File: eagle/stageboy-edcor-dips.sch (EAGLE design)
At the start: 38 parts, among them IC1 MEGA8-P, IC2 7805TV, J2 DCJ0202, Q1 16MHz, X1 MIDI IN, X2 MIDI OUT, X4 22-23-2021, X6 GBIO

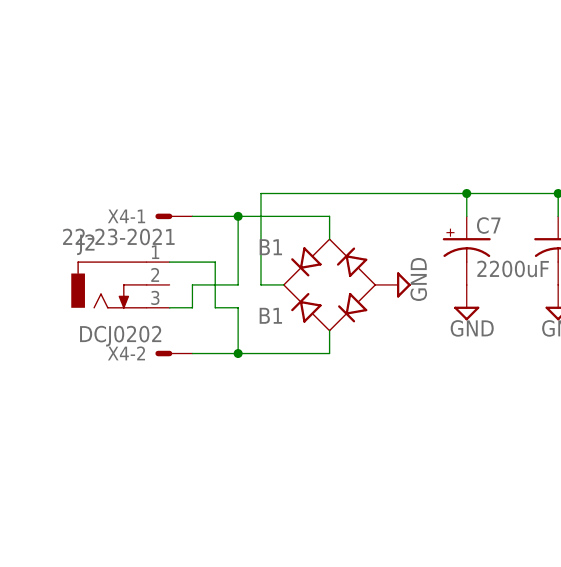
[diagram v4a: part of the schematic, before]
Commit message: Swapped out DC jack
Swapped DC jack out for one that uses large vias, as OshPark
doesn't do plated cutouts. Looks like most any DC jack will do,
but the part swapped was one from the SparkFun library.
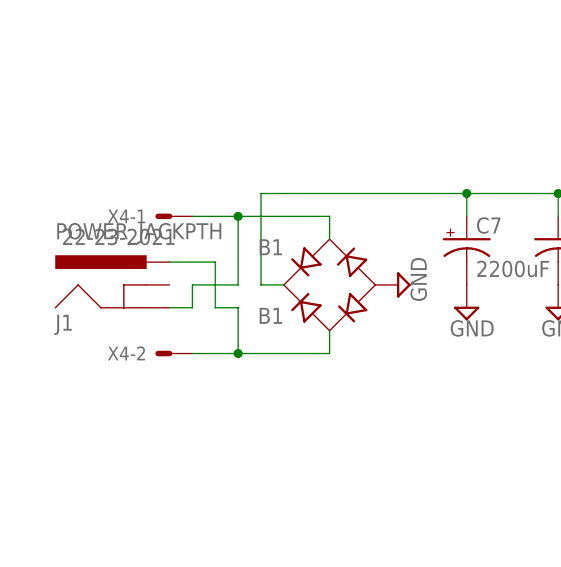
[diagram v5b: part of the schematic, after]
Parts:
- removed J2: DCJ0202, con-jack:DCJ0202
- added J1: POWER_JACKPTH, SparkFun-Connectors:POWER_JACKPTH
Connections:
- net N$38: now also J1.GND; no longer J2.3
- net N$39: now also J1.PWR; no longer J2.1
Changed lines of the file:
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@@
 <grid distance="0.1" unitdist="inch" unit="inch" style="lines" multiple="1" display="no" altdistance="0.01" altunitdist="inch" altunit="inch"/>
 <layers>
-<layer number="1" name="Top" color="4" fill="1" visible="no" active="no"/>
-<layer number="2" name="Route2" color="1" fill="3" visible="no" active="no"/>
-<layer number="3" name="Route3" color="4" fill="3" visible="no" active="no"/>
-<layer number="14" name="Route14" color="1" fill="6" visible="no" active="no"/>
-<layer number="15" name="Route15" color="4" fill="6" visible="no" active="no"/>
-<layer number="16" name="Bottom" color="1" fill="1" visible="no" active="no"/>
-<layer number="17" name="Pads" color="2" fill="1" visible="no" active="no"/>
-<layer number="18" name="Vias" color="2" fill="1" visible="no" active="no"/>
-<layer number="19" name="Unrouted" color="6" fill="1" visible="no" active="no"/>
-<layer number="20" name="Dimension" color="15" fill="1" visible="no" active="no"/>
-<layer number="21" name="tPlace" color="7" fill="1" visible="no" active="no"/>
-<layer number="22" name="bPlace" color="7" fill="1" visible="no" active="no"/>
-<layer number="23" name="tOrigins" color="15" fill="1" visible="no" active="no"/>
-<layer number="24" name="bOrigins" color="15" fill="1" visible="no" active="no"/>
-<layer number="25" name="tNames" color="7" fill="1" visible="no" active="no"/>
-<layer number="26" name="bNames" color="7" fill="1" visible="no" active="no"/>
-<layer number="27" name="tValues" color="7" fill="1" visible="no" active="no"/>
-<layer number="28" name="bValues" color="7" fill="1" visible="no" active="no"/>
+<layer number="1" name="Top" color="4" fill="1" visible="yes" active="no"/>
+<layer number="2" name="Route2" color="1" fill="3" visible="yes" active="no"/>
+<layer number="3" name="Route3" color="4" fill="3" visible="yes" active="no"/>
+<layer number="14" name="Route14" color="1" fill="6" visible="yes" active="no"/>
+<layer number="15" name="Route15" color="4" fill="6" visible="yes" active="no"/>
+<layer number="16" name="Bottom" color="1" fill="1" visible="yes" active="no"/>
+<layer number="17" name="Pads" color="2" fill="1" visible="yes" active="no"/>
+<layer number="18" name="Vias" color="2" fill="1" visible="yes" active="no"/>
+<layer number="19" name="Unrouted" color="6" fill="1" visible="yes" active="no"/>
+<layer number="20" name="Dimension" color="15" fill="1" visible="yes" active="no"/>
+<layer number="21" name="tPlace" color="7" fill="1" visible="yes" active="no"/>
+<layer number="22" name="bPlace" color="7" fill="1" visible="yes" active="no"/>
+<layer number="23" name="tOrigins" color="15" fill="1" visible="yes" active="no"/>
+<layer number="24" name="bOrigins" color="15" fill="1" visible="yes" active="no"/>
+<layer number="25" name="tNames" color="7" fill="1" visible="yes" active="no"/>
+<layer number="26" name="bNames" color="7" fill="1" visible="yes" active="no"/>
+<layer number="27" name="tValues" color="7" fill="1" visible="yes" active="no"/>
+<layer number="28" name="bValues" color="7" fill="1" visible="yes" active="no"/>
 <layer number="29" name="tStop" color="7" fill="3" visible="no" active="no"/>
 <layer number="30" name="bStop" color="7" fill="6" visible="no" active="no"/>
@@
 <layer number="35" name="tGlue" color="7" fill="4" visible="no" active="no"/>
 <layer number="36" name="bGlue" color="7" fill="5" visible="no" active="no"/>
-<layer number="37" name="tTest" color="7" fill="1" visible="no" active="no"/>
-<layer number="38" name="bTest" color="7" fill="1" visible="no" active="no"/>
+<layer number="37" name="tTest" color="7" fill="1" visible="yes" active="no"/>
+<layer number="38" name="bTest" color="7" fill="1" visible="yes" active="no"/>
 <layer number="39" name="tKeepout" color="4" fill="11" visible="no" active="no"/>
 <layer number="40" name="bKeepout" color="1" fill="11" visible="no" active="no"/>
@@
 <layer number="44" name="Drills" color="7" fill="1" visible="no" active="no"/>
 <layer number="45" name="Holes" color="7" fill="1" visible="no" active="no"/>
-<layer number="46" name="Milling" color="3" fill="1" visible="no" active="no"/>
-<layer number="47" name="Measures" color="7" fill="1" visible="no" active="no"/>
-<layer number="48" name="Document" color="7" fill="1" visible="no" active="no"/>
-<layer number="49" name="Reference" color="7" fill="1" visible="no" active="no"/>
-<layer number="50" name="dxf" color="7" fill="1" visible="no" active="no"/>
-<layer number="51" name="tDocu" color="7" fill="1" visible="no" active="no"/>
-<layer number="52" name="bDocu" color="7" fill="1" visible="no" active="no"/>
-<layer number="53" name="tGND_GNDA" color="7" fill="9" visible="no" active="no"/>
-<layer number="54" name="bGND_GNDA" color="1" fill="9" visible="no" active="no"/>
-<layer number="56" name="wert" color="7" fill="1" visible="no" active="no"/>
+<layer number="46" name="Milling" color="3" fill="1" visible="yes" active="no"/>
+<layer number="47" name="Measures" color="7" fill="1" visible="yes" active="no"/>
+<layer number="48" name="Document" color="7" fill="1" visible="yes" active="no"/>
+<layer number="49" name="Reference" color="7" fill="1" visible="yes" active="no"/>
+<layer number="50" name="dxf" color="7" fill="1" visible="yes" active="no"/>
+<layer number="51" name="tDocu" color="7" fill="1" visible="yes" active="no"/>
+<layer number="52" name="bDocu" color="7" fill="1" visible="yes" active="no"/>
+<layer number="53" name="tGND_GNDA" color="7" fill="9" visible="yes" active="no"/>
+<layer number="54" name="bGND_GNDA" color="1" fill="9" visible="yes" active="no"/>
+<layer number="56" name="wert" color="7" fill="1" visible="yes" active="no"/>
 <layer number="91" name="Nets" color="2" fill="1" visible="yes" active="yes"/>
 <layer number="92" name="Busses" color="1" fill="1" visible="yes" active="yes"/>
@@
 <layer number="106" name="bPlate" color="7" fill="1" visible="no" active="yes"/>
 <layer number="107" name="Crop" color="7" fill="1" visible="no" active="yes"/>
+<layer number="108" name="tplace-old" color="10" fill="1" visible="yes" active="yes"/>
+<layer number="109" name="ref-old" color="11" fill="1" visible="yes" active="yes"/>
 <layer number="116" name="Patch_BOT" color="9" fill="4" visible="no" active="yes"/>
 <layer number="121" name="_tsilk" color="7" fill="1" visible="no" active="yes"/>
@@
 <layer number="144" name="Drill_legend" color="7" fill="1" visible="no" active="yes"/>
 <layer number="151" name="HeatSink" color="7" fill="1" visible="no" active="yes"/>
+<layer number="199" name="Contour" color="7" fill="1" visible="yes" active="yes"/>
 <layer number="200" name="200bmp" color="1" fill="10" visible="no" active="yes"/>
 <layer number="201" name="201bmp" color="2" fill="10" visible="no" active="yes"/>
@@
 <part name="SUPPLY29" library="supply2" deviceset="GND" device=""/>
 <part name="5VDC" library="con-molex" deviceset="22-23-2021" device="" value="DCPWR"/>
-<part name="J2" library="con-jack" deviceset="DCJ0202" device=""/>
+<part name="J1" library="SparkFun-Connectors" deviceset="POWER_JACK" device="PTH"/>
 </parts>
 <sheets>
@@
 <instance part="5VDC" gate="-1" x="101.6" y="139.7"/>
 <instance part="5VDC" gate="-2" x="101.6" y="137.16"/>
-<instance part="J2" gate="G$1" x="-17.78" y="114.3"/>
+<instance part="J1" gate="G$1" x="-12.7" y="109.22"/>
 </instances>
 <busses>
@@
 <wire x1="-2.54" y1="114.3" x2="-7.62" y2="114.3" width="0.1524" layer="91"/>
 <wire x1="-7.62" y1="114.3" x2="-7.62" y2="111.76" width="0.1524" layer="91"/>
-<pinref part="J2" gate="G$1" pin="3"/>
 <wire x1="-7.62" y1="111.76" x2="-10.16" y2="111.76" width="0.1524" layer="91"/>
+<pinref part="J1" gate="G$1" pin="GND"/>
 </segment>
 </net>
@@
 <wire x1="-7.62" y1="106.68" x2="-2.54" y2="106.68" width="0.1524" layer="91"/>
 <junction x="-2.54" y="106.68"/>
-<pinref part="J2" gate="G$1" pin="1"/>
 <wire x1="-10.16" y1="116.84" x2="-5.08" y2="116.84" width="0.1524" layer="91"/>
 <wire x1="-5.08" y1="116.84" x2="-5.08" y2="111.76" width="0.1524" layer="91"/>
 <wire x1="-5.08" y1="111.76" x2="-2.54" y2="111.76" width="0.1524" layer="91"/>
-</segment>
-</net>
+<pinref part="J1" gate="G$1" pin="PWR"/>
+</segment>
+</net>
